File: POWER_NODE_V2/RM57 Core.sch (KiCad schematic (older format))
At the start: 0 parts

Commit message: Power Node V2 WIP
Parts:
- added J?: I2C2_J10_8_9, symbol CONN_01X02
- added J?: Booster_J1_J3, symbol Booster_J1_J3
- added J?: Booster_J4_J2, symbol Booster_J4_J2
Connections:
- net BATT_VOLT: now also J?.26 (P26)
- net BMS_ALERT: now also J?.11 (P11)
- net BMS_CONV: now also J?.33 (P33)
- net BMS_DRDY: now also J?.31 (P31)
- net BMS_FAN: now also J?.34 (P34)
- net BMS_FAULT: now also J?.32 (P32)
- net BMS_MISO: now also J?.14 (P14)
- net BMS_MOSI: now also J?.15 (P15)
- net BMS_NCS: now also J?.18 (P18)
- net BMS_SCK: now also J?.7 (P7)
- net CHG_RLY: now also J?.8 (P8)
- net CHG_VOLT: now also J?.23 (P23)
- net DC_WATCHDOG: now also J?.17 (P17)
- net RM57_I2C1_SCL: now also J?.12 (P12)
- net RM57_I2C1_SDA: now also J?.13 (P13)
- net RM57_I2C2_SDA: now also J?.2 (P2)
- new net BATT_I: J?.28 (P28)
- new net BATT_I_REF: J?.27 (P27)
- new net BMS_COMMS_EN: J?.5 (P5)
- new net CHG_I: J?.25 (P25)
- new net CHG_I_REF: J?.24 (P24)
- new net RM57_I2C2_SCL: J?.1 (P1)
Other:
- note added: "8"
- note added: "9"
- note added: "TODO: BMS GIO may be rearranged\nas needed for layout"
- note added: "TODO: Power through header"
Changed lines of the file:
@@
 $Descr A4 11693 8268
 encoding utf-8
-Sheet 5 8
+Sheet 4 8
 Title ""
 Date ""
@@
 Comment4 ""
 $EndDescr
-Text HLabel 4100 4550 0    60   Output ~ 0
-RM57_CAN_TX
-Text HLabel 4100 4650 0    60   Input ~ 0
-RM57_CAN_RX
-Text HLabel 4100 4050 0    60   Output ~ 0
+Text HLabel 3700 3200 0    60   Output ~ 0
 CHG_RLY
-Text HLabel 4100 4150 0    60   Input ~ 0
-CHG_CURRENT
-Text HLabel 4100 4250 0    60   Input ~ 0
+Text HLabel 5200 2800 2    60   Input ~ 0
+CHG_I_REF
+Text HLabel 5200 2700 2    60   Input ~ 0
 CHG_VOLT
-Text HLabel 4100 4350 0    60   Input ~ 0
+Text HLabel 5200 3000 2    60   Input ~ 0
 BATT_VOLT
-Text HLabel 4100 2750 0    60   Output ~ 0
+Text HLabel 7950 2800 2    60   Output ~ 0
 DC_WATCHDOG
-Text HLabel 4100 2950 0    60   Output ~ 0
+Text HLabel 3700 3100 0    60   Output ~ 0
 BMS_SCK
-Text HLabel 4100 3050 0    60   Output ~ 0
+Text HLabel 7950 3000 2    60   Output ~ 0
 BMS_MOSI
-Text HLabel 4100 3250 0    60   Output ~ 0
+Text HLabel 7950 2700 2    60   Output ~ 0
 BMS_NCS
-Text HLabel 4100 3150 0    60   Output ~ 0
+Text HLabel 7950 3100 2    60   Input ~ 0
 BMS_MISO
-Text HLabel 4100 3350 0    60   Input ~ 0
+Text HLabel 6850 3400 0    60   Input ~ 0
 BMS_DRDY
-Text HLabel 4100 3450 0    60   Output ~ 0
-BMS_COMMS_ON
-Text HLabel 4100 3550 0    60   Output ~ 0
+Text HLabel 3700 2900 0    60   Output ~ 0
+BMS_COMMS_EN
+Text HLabel 6850 3200 0    60   Output ~ 0
 BMS_CONV
-Text HLabel 4100 2150 0    60   Output ~ 0
+Text HLabel 7950 3200 2    60   Output ~ 0
 RM57_I2C1_SDA
-Text HLabel 4100 2250 0    60   Output ~ 0
+Text HLabel 7950 3300 2    60   Output ~ 0
 RM57_I2C1_SCL
-Text HLabel 4100 2450 0    60   Output ~ 0
+Text HLabel 4150 4100 0    60   Output ~ 0
 RM57_I2C2_SDA
-Text HLabel 4100 2550 0    60   Output ~ 0
-RM57_I2C2_SDC
-Text HLabel 4100 3850 0    60   Output ~ 0
+Text HLabel 4150 3950 0    60   Output ~ 0
+RM57_I2C2_SCL
+Text HLabel 6850 3100 0    60   Output ~ 0
 BMS_FAN
-Text HLabel 4100 3650 0    60   Input ~ 0
+Text HLabel 6850 3300 0    60   Input ~ 0
 BMS_FAULT
-Text HLabel 4100 3750 0    60   Input ~ 0
+Text HLabel 7950 3400 2    60   Input ~ 0
 BMS_ALERT
+$Comp
+L CONN_01X02 J?
+U 1 1 5950A33D
+P 4700 4000
+F 0 "J?" H 4700 4150 50  0000 C CNN
+F 1 "I2C2_J10_8_9" V 4800 4000 50  0000 C CNN
+F 2 "" H 4700 4000 50  0001 C CNN
+F 3 "" H 4700 4000 50  0001 C CNN
+	1    4700 4000
+	1    0    0    -1
+$EndComp
+$Comp
+L Booster_J1_J3 J?
+U 1 1 5950AD17
+P 4650 2950
+F 0 "J?" H 4650 3500 50  0000 C CNN
+F 1 "Booster_J1_J3" V 4650 2950 50  0000 C CNN
+F 2 "" H 4650 1750 50  0001 C CNN
+F 3 "" H 4650 1750 50  0001 C CNN
+	1    4650 2950
+	1    0    0    -1
+$EndComp
+$Comp
+L Booster_J4_J2 J?
+U 1 1 5950B1BF
+P 7250 2950
+F 0 "J?" H 7250 3500 50  0000 C CNN
+F 1 "Booster_J4_J2" V 7250 2950 50  0000 C CNN
+F 2 "" H 7250 1750 50  0001 C CNN
+F 3 "" H 7250 1750 50  0001 C CNN
+	1    7250 2950
+	1    0    0    -1
+$EndComp
+Wire Wire Line
+	7950 3300 7500 3300
+Wire Wire Line
+	7500 3200 7950 3200
+Wire Wire Line
+	7950 3100 7500 3100
+Wire Wire Line
+	7500 3000 7950 3000
+Wire Wire Line
+	7950 2700 7500 2700
+Wire Wire Line
+	3700 3100 4400 3100
+Wire Wire Line
+	4500 3950 4150 3950
+Wire Wire Line
+	4150 4100 4500 4100
+Wire Wire Line
+	4500 4100 4500 4050
+Text Notes 4450 3900 0    60   ~ 0
+8
+Text Notes 4450 4250 0    60   ~ 0
+9
+Text HLabel 5200 2900 2    60   Input ~ 0
+CHG_I
+Text HLabel 5200 3100 2    60   Input ~ 0
+BATT_I_REF
+Text HLabel 5200 3200 2    60   Input ~ 0
+BATT_I
+Text Notes 6350 3950 0    79   ~ 0
+TODO: BMS GIO may be rearranged\nas needed for layout
+Wire Wire Line
+	6850 3100 7000 3100
+Wire Wire Line
+	7000 3200 6850 3200
+Wire Wire Line
+	6850 3300 7000 3300
+Wire Wire Line
+	7000 3400 6850 3400
+Wire Wire Line
+	7500 3400 7950 3400
+Wire Wire Line
+	4900 3200 5200 3200
+Wire Wire Line
+	5200 3100 4900 3100
+Wire Wire Line
+	4900 3000 5200 3000
+Wire Wire Line
+	5200 2900 4900 2900
+Wire Wire Line
+	4900 2800 5200 2800
+Wire Wire Line
+	5200 2700 4900 2700
+Wire Wire Line
+	7950 2800 7500 2800
+Wire Wire Line
+	3700 2900 4400 2900
+Text Notes 4750 1850 0    118  ~ 0
+TODO: Power through header
+Wire Wire Line
+	3700 3200 4400 3200
 $EndSCHEMATC

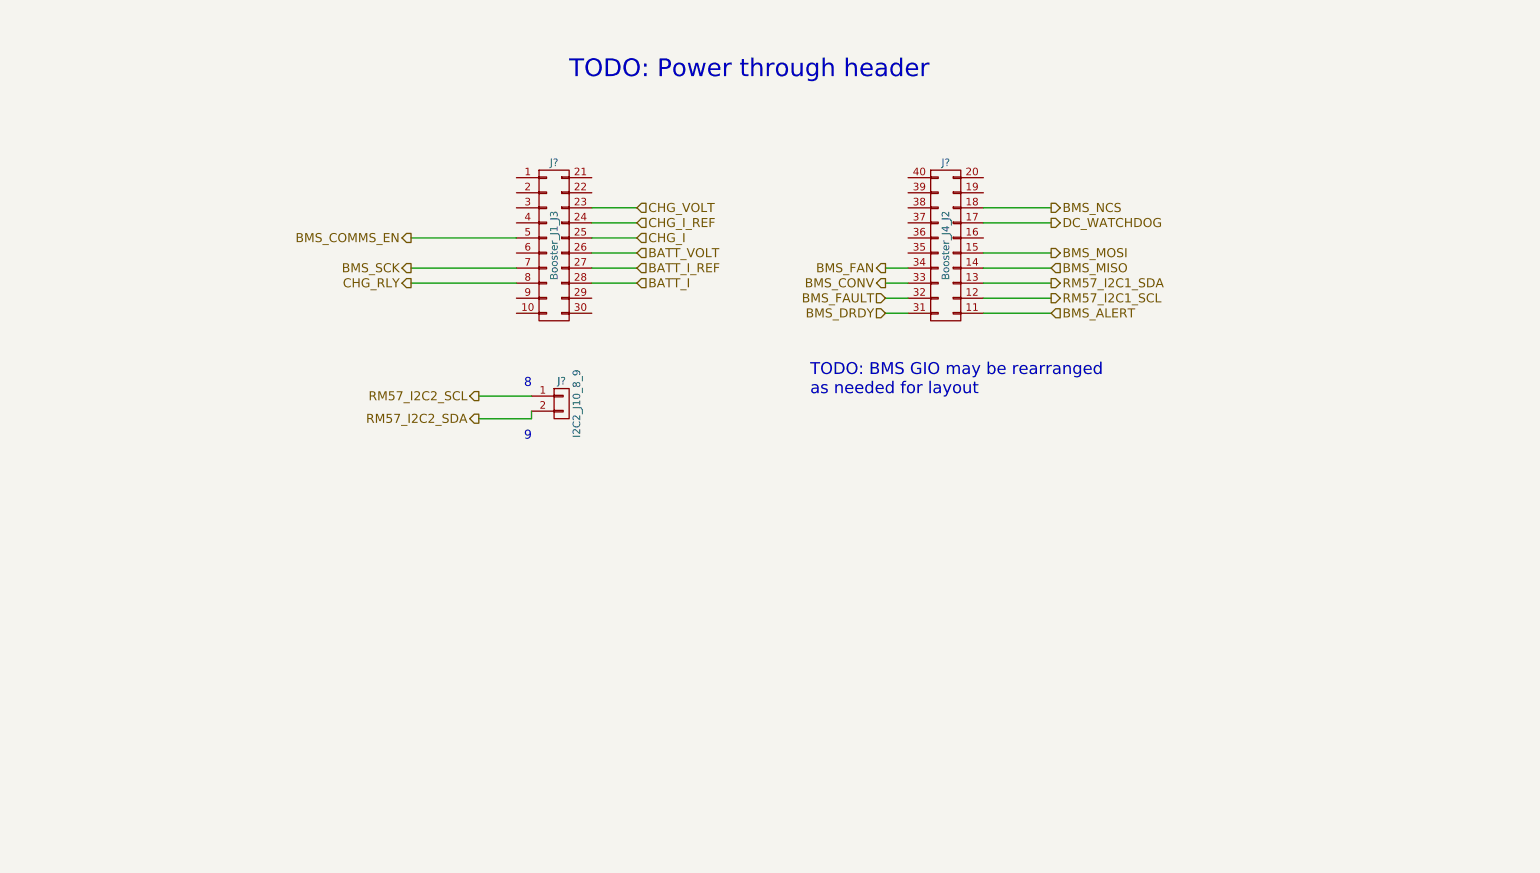
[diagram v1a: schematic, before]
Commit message: Schematic for Power Node V2 mostly done - mostly need connectors
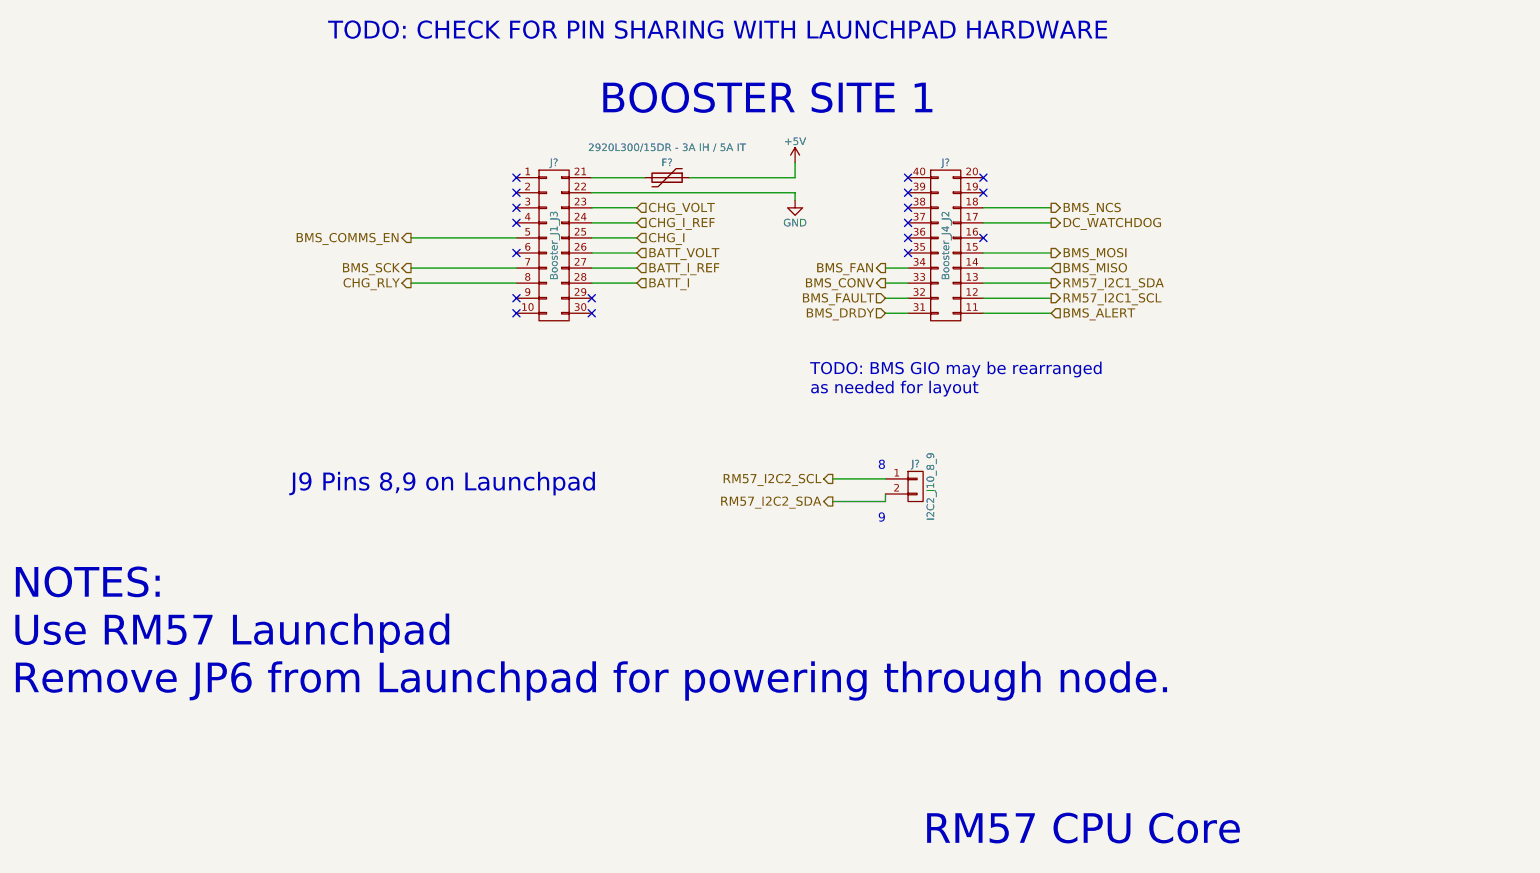
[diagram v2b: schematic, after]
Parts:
- added F?: 2920L300/15DR - 3A IH / 5A IT, symbol Polyfuse
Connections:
- net at J?.21 (P21): now also F?.2
- net GND: now reaches J?.22 (P22)
- new net +5V: F?.1
- no-connect marks 0 -> 18
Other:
- note added: "BOOSTER SITE 1"
- note added: "J9 Pins 8,9 on Launchpad"
- note added: "NOTES:\nUse RM57 Launchpad\nRemove JP6 from Launchpad for powering through node."
- note added: "RM57 CPU Core"
- note added: "TODO: CHECK FOR PIN SHARING WITH LAUNCHPAD HARDWARE"
- note removed: "TODO: Power through header"
- moved on the sheet: J?
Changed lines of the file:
@@
 $Descr A4 11693 8268
 encoding utf-8
-Sheet 4 8
+Sheet 4 9
 Title ""
 Date ""
@@
 Text HLabel 7950 3300 2    60   Output ~ 0
 RM57_I2C1_SCL
-Text HLabel 4150 4100 0    60   Output ~ 0
+Text HLabel 6500 4650 0    60   Output ~ 0
 RM57_I2C2_SDA
-Text HLabel 4150 3950 0    60   Output ~ 0
+Text HLabel 6500 4500 0    60   Output ~ 0
 RM57_I2C2_SCL
 Text HLabel 6850 3100 0    60   Output ~ 0
@@
 L CONN_01X02 J?
 U 1 1 5950A33D
-P 4700 4000
-F 0 "J?" H 4700 4150 50  0000 C CNN
-F 1 "I2C2_J10_8_9" V 4800 4000 50  0000 C CNN
-F 2 "" H 4700 4000 50  0001 C CNN
-F 3 "" H 4700 4000 50  0001 C CNN
-	1    4700 4000
+P 7050 4550
+F 0 "J?" H 7050 4700 50  0000 C CNN
+F 1 "I2C2_J10_8_9" V 7150 4550 50  0000 C CNN
+F 2 "" H 7050 4550 50  0001 C CNN
+F 3 "" H 7050 4550 50  0001 C CNN
+	1    7050 4550
 	1    0    0    -1
 $EndComp
@@
 	3700 3100 4400 3100
 Wire Wire Line
-	4500 3950 4150 3950
-Wire Wire Line
-	4150 4100 4500 4100
-Wire Wire Line
-	4500 4100 4500 4050
-Text Notes 4450 3900 0    60   ~ 0
+	6850 4500 6500 4500
+Wire Wire Line
+	6500 4650 6850 4650
+Wire Wire Line
+	6850 4650 6850 4600
+Text Notes 6800 4450 0    60   ~ 0
 8
-Text Notes 4450 4250 0    60   ~ 0
+Text Notes 6800 4800 0    60   ~ 0
 9
 Text HLabel 5200 2900 2    60   Input ~ 0
@@
 Wire Wire Line
 	3700 2900 4400 2900
-Text Notes 4750 1850 0    118  ~ 0
-TODO: Power through header
+Text Notes 3150 1600 0    118  ~ 0
+TODO: CHECK FOR PIN SHARING WITH LAUNCHPAD HARDWARE
 Wire Wire Line
 	3700 3200 4400 3200
+Text Notes 7100 6950 0    197  ~ 0
+RM57 CPU Core
+Text Notes 1050 5950 0    197  ~ 0
+NOTES:\nUse RM57 Launchpad\nRemove JP6 from Launchpad for powering through node.
+NoConn ~ 4400 2500
+NoConn ~ 4400 2600
+NoConn ~ 4400 2800
+NoConn ~ 4400 2700
+NoConn ~ 4400 3000
+NoConn ~ 4400 3300
+NoConn ~ 4400 3400
+NoConn ~ 4900 3400
+NoConn ~ 4900 3300
+$Comp
+L +5V #PWR?
+U 1 1 59521447
+P 6250 2400
+F 0 "#PWR?" H 6250 2250 50  0001 C CNN
+F 1 "+5V" H 6250 2540 50  0000 C CNN
+F 2 "" H 6250 2400 50  0001 C CNN
+F 3 "" H 6250 2400 50  0001 C CNN
+	1    6250 2400
+	1    0    0    -1
+$EndComp
+NoConn ~ 7000 3000
+NoConn ~ 7000 2900
+NoConn ~ 7000 2800
+NoConn ~ 7000 2700
+NoConn ~ 7000 2600
+NoConn ~ 7000 2500
+NoConn ~ 7500 2500
+NoConn ~ 7500 2600
+NoConn ~ 7500 2900
+$Comp
+L Polyfuse F?
+U 1 1 595214F2
+P 5400 2500
+F 0 "F?" V 5300 2500 50  0000 C CNN
+F 1 "2920L300/15DR - 3A IH / 5A IT" V 5200 2500 50  0000 C CNN
+F 2 "" H 5450 2300 50  0001 L CNN
+F 3 "" H 5400 2500 50  0001 C CNN
+	1    5400 2500
+	0    1    1    0
+$EndComp
+Wire Wire Line
+	4900 2500 5250 2500
+Wire Wire Line
+	5550 2500 6250 2500
+Wire Wire Line
+	6250 2500 6250 2400
+$Comp
+L GND #PWR?
+U 1 1 59521ACA
+P 6250 2650
+F 0 "#PWR?" H 6250 2400 50  0001 C CNN
+F 1 "GND" H 6250 2500 50  0000 C CNN
+F 2 "" H 6250 2650 50  0001 C CNN
+F 3 "" H 6250 2650 50  0001 C CNN
+	1    6250 2650
+	1    0    0    -1
+$EndComp
+Wire Wire Line
+	6250 2600 4900 2600
+Wire Wire Line
+	6250 2650 6250 2600
+Text Notes 4950 2100 0    197  ~ 0
+BOOSTER SITE 1
+Text Notes 2900 4600 0    118  ~ 0
+J9 Pins 8,9 on Launchpad
 $EndSCHEMATC

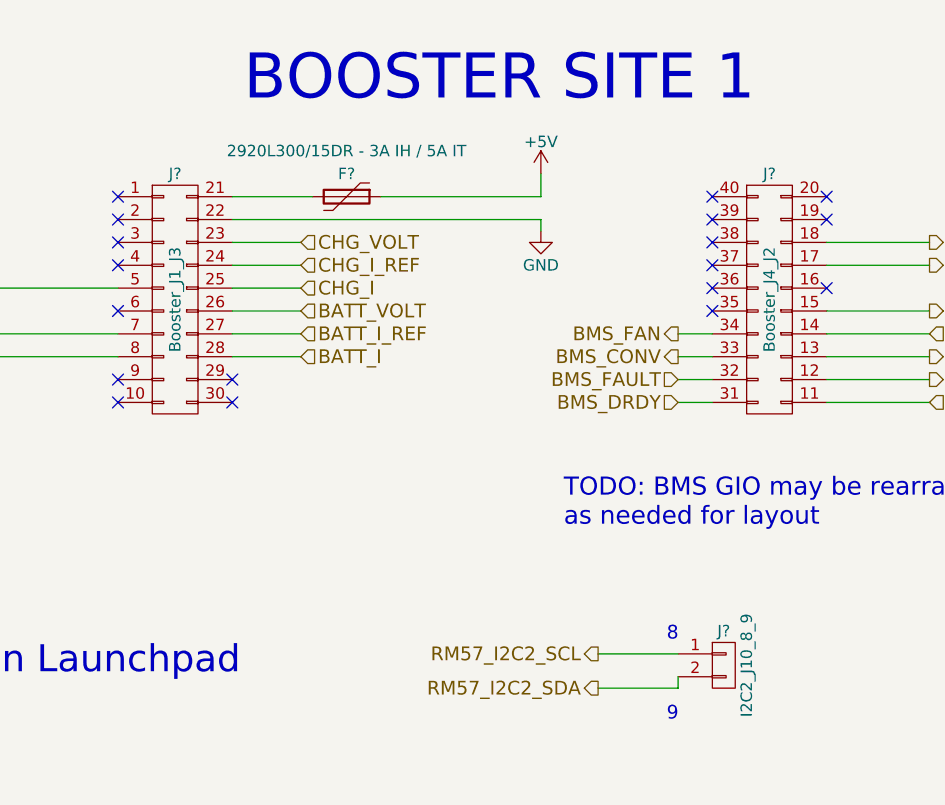
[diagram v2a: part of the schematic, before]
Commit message: made a lot of footprints, began PCB layout for power node v2
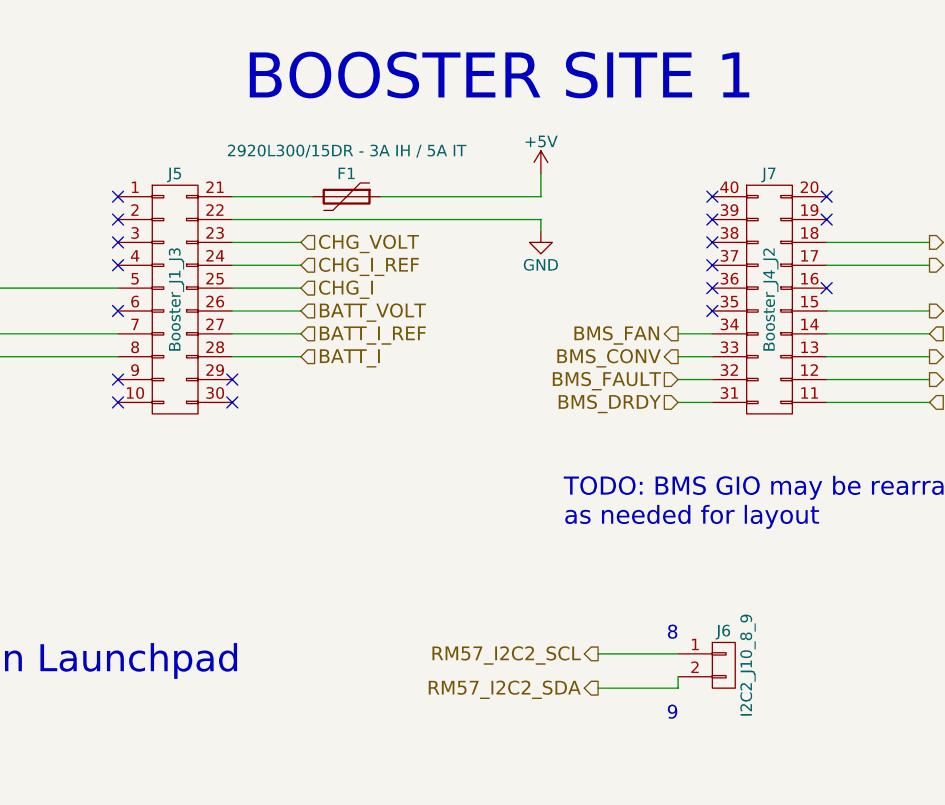
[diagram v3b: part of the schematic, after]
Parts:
- F1: renamed from F?; footprint (none) -> rLoop Footprints:2920L300_15DR
- J5, J7: renamed from J?; footprint (none) -> Pin_Headers:Pin_Header_Straight_2x10_Pitch2.54mm
- J6: renamed from J?; footprint (none) -> Pin_Headers:Pin_Header_Straight_1x02_Pitch2.54mm
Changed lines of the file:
@@
 BMS_ALERT
 $Comp
-L CONN_01X02 J?
+L CONN_01X02 J6
 U 1 1 5950A33D
 P 7050 4550
-F 0 "J?" H 7050 4700 50  0000 C CNN
+F 0 "J6" H 7050 4700 50  0000 C CNN
 F 1 "I2C2_J10_8_9" V 7150 4550 50  0000 C CNN
-F 2 "" H 7050 4550 50  0001 C CNN
+F 2 "Pin_Headers:Pin_Header_Straight_1x02_Pitch2.54mm" H 7050 4550 50  0001 C CNN
 F 3 "" H 7050 4550 50  0001 C CNN
 	1    7050 4550
@@
 $EndComp
 $Comp
-L Booster_J1_J3 J?
+L Booster_J1_J3 J5
 U 1 1 5950AD17
 P 4650 2950
-F 0 "J?" H 4650 3500 50  0000 C CNN
+F 0 "J5" H 4650 3500 50  0000 C CNN
 F 1 "Booster_J1_J3" V 4650 2950 50  0000 C CNN
-F 2 "" H 4650 1750 50  0001 C CNN
+F 2 "Pin_Headers:Pin_Header_Straight_2x10_Pitch2.54mm" H 4650 1750 50  0001 C CNN
 F 3 "" H 4650 1750 50  0001 C CNN
 	1    4650 2950
@@
 $EndComp
 $Comp
-L Booster_J4_J2 J?
+L Booster_J4_J2 J7
 U 1 1 5950B1BF
 P 7250 2950
-F 0 "J?" H 7250 3500 50  0000 C CNN
+F 0 "J7" H 7250 3500 50  0000 C CNN
 F 1 "Booster_J4_J2" V 7250 2950 50  0000 C CNN
-F 2 "" H 7250 1750 50  0001 C CNN
+F 2 "Pin_Headers:Pin_Header_Straight_2x10_Pitch2.54mm" H 7250 1750 50  0001 C CNN
 F 3 "" H 7250 1750 50  0001 C CNN
 	1    7250 2950
@@
 NoConn ~ 4900 3300
 $Comp
-L +5V #PWR?
+L +5V #PWR030
 U 1 1 59521447
 P 6250 2400
-F 0 "#PWR?" H 6250 2250 50  0001 C CNN
+F 0 "#PWR030" H 6250 2250 50  0001 C CNN
 F 1 "+5V" H 6250 2540 50  0000 C CNN
 F 2 "" H 6250 2400 50  0001 C CNN
@@
 NoConn ~ 7500 2900
 $Comp
-L Polyfuse F?
+L Polyfuse F1
 U 1 1 595214F2
 P 5400 2500
-F 0 "F?" V 5300 2500 50  0000 C CNN
+F 0 "F1" V 5300 2500 50  0000 C CNN
 F 1 "2920L300/15DR - 3A IH / 5A IT" V 5200 2500 50  0000 C CNN
-F 2 "" H 5450 2300 50  0001 L CNN
+F 2 "rLoop Footprints:2920L300_15DR" H 5450 2300 50  0001 L CNN
 F 3 "" H 5400 2500 50  0001 C CNN
 	1    5400 2500
@@
 	6250 2500 6250 2400
 $Comp
-L GND #PWR?
+L GND #PWR031
 U 1 1 59521ACA
 P 6250 2650
-F 0 "#PWR?" H 6250 2400 50  0001 C CNN
+F 0 "#PWR031" H 6250 2400 50  0001 C CNN
 F 1 "GND" H 6250 2500 50  0000 C CNN
 F 2 "" H 6250 2650 50  0001 C CNN
